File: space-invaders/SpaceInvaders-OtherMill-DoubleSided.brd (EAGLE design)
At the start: 101.6 x 95.2 mm, 26 parts, among them J2-J4 TM4C123GXL, J3-J1 TM4C123GXL, J5 Nokia_5110, J6 Nokia_5110, J7 9V, U1 LM7805CT

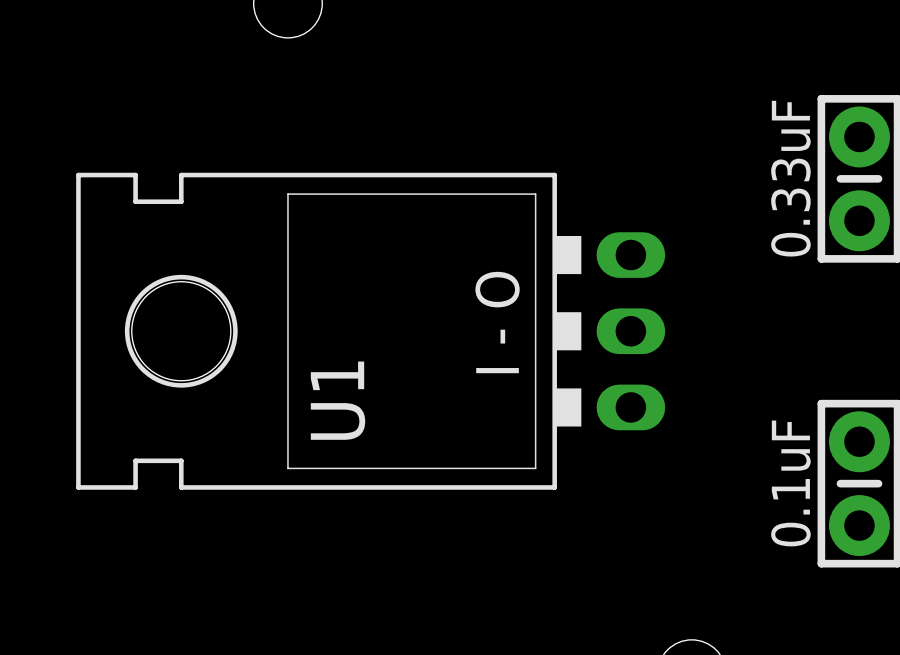
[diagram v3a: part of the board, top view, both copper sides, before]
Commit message: Connect nets & Apply schematic convention
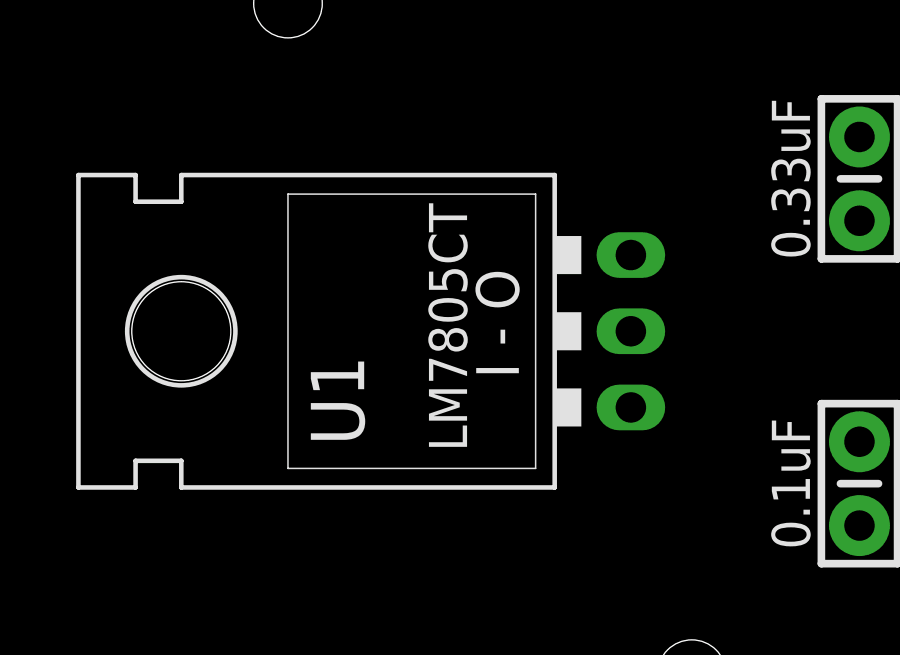
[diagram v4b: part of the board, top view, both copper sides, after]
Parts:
- J5, J6: value Nokia_5110 -> NOKIA_5110
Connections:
- removed net D/C: J6.5
- removed net DN<MOSI>: J6.6
- removed net PE0: J2-J4.6, R2.P$2, S2.3
- removed net RST: J6.4
- removed net SCE: J5.3
- removed net SCLK: J5.7
- new net DAC: J2-J4.4, J2-J4.5, J3-J1.14, J3-J1.16, R10.P$1, R11.P$1, R6.P$1, R7.P$1, R9.P$1
- net PA2: now also J5.7
- net PA3: now also J5.3
- net PA5: now also J6.6
- net PA6: now also J6.5
- net PA7: now also J6.4
- net PB2: now also J2-J4.6, R2.P$2, S2.3; no longer J2-J4.4, J2-J4.5, J3-J1.14, J3-J1.16, R10.P$1, R11.P$1, R6.P$1, R7.P$1, R9.P$1
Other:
- board text added: "LM7805CT"
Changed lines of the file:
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@@
 <?xml version="1.0" encoding="utf-8"?>
 <!DOCTYPE eagle SYSTEM "eagle.dtd">
-<eagle version="8.0.0">
+<eagle version="8.0.1">
 <drawing>
 <settings>
@@
 <text x="77.47" y="57.15" size="1.27" layer="21" font="vector" ratio="10" align="center">220</text>
 <text x="23.495" y="80.264" size="1.4224" layer="21" font="vector" ratio="10" rot="R90" align="center">I - O</text>
+<text x="21.844" y="80.137" size="1.27" layer="21" ratio="10" rot="R90" align="center">LM7805CT</text>
 </plain>
 <attributes>
@@
 <autorouter>
 <pass name="Default">
-<param name="RoutingGrid" value="6.25mil"/>
+<param name="RoutingGrid" value="50mil"/>
 <param name="AutoGrid" value="1"/>
 <param name="Efforts" value="2"/>
 <param name="TopRouterVariant" value="1"/>
 <param name="tpViaShape" value="round"/>
-<param name="PrefDir.1" value="*"/>
+<param name="PrefDir.1" value="a"/>
 <param name="PrefDir.2" value="0"/>
 <param name="PrefDir.3" value="0"/>
@@
 <param name="PrefDir.14" value="0"/>
 <param name="PrefDir.15" value="0"/>
-<param name="PrefDir.16" value="-"/>
+<param name="PrefDir.16" value="a"/>
 <param name="cfVia" value="8"/>
 <param name="cfNonPref" value="5"/>
@@
 <element name="J2-J4" library="SparkFun-Connectors" package="2X10" value="TM4C123GXL" x="48.26" y="63.5" rot="R270"/>
 <element name="J3-J1" library="SparkFun-Connectors" package="2X10" value="TM4C123GXL" x="7.62" y="40.64" rot="R90"/>
-<element name="J5" library="SparkFun-Connectors" package="1X08" value="Nokia_5110" x="68.58" y="71.12">
+<element name="J5" library="SparkFun-Connectors" package="1X08" value="NOKIA_5110" x="68.58" y="71.12">
 <attribute name="PROD_ID" value="CONN-08438" x="68.58" y="71.12" size="1.778" layer="27" display="off"/>
 </element>
-<element name="J6" library="SparkFun-Connectors" package="1X08" value="Nokia_5110" x="68.58" y="30.48">
+<element name="J6" library="SparkFun-Connectors" package="1X08" value="NOKIA_5110" x="68.58" y="30.48">
 <attribute name="PROD_ID" value="CONN-08438" x="68.58" y="30.48" size="1.778" layer="27" display="off"/>
 </element>
@@
 <contactref element="J6" pad="7"/>
 <contactref element="J2-J4" pad="20"/>
+<contactref element="J5" pad="7"/>
+<wire x1="83.82" y1="30.48" x2="83.82" y2="71.12" width="0" layer="19" extent="1-1"/>
 <wire x1="50.8" y1="40.64" x2="83.82" y2="30.48" width="0" layer="19" extent="1-1"/>
 </signal>
@@
 <contactref element="J3-J1" pad="2"/>
 <contactref element="J5" pad="4"/>
-<wire x1="5.08" y1="40.64" x2="76.2" y2="71.12" width="0" layer="19" extent="1-1"/>
+<contactref element="J6" pad="4"/>
+<wire x1="76.2" y1="30.48" x2="76.2" y2="71.12" width="0" layer="19" extent="1-1"/>
+<wire x1="5.08" y1="40.64" x2="76.2" y2="30.48" width="0" layer="19" extent="1-1"/>
 </signal>
 <signal name="PA6">
 <contactref element="J3-J1" pad="4"/>
 <contactref element="J5" pad="5"/>
-<wire x1="5.08" y1="43.18" x2="78.74" y2="71.12" width="0" layer="19" extent="1-1"/>
+<contactref element="J6" pad="5"/>
+<wire x1="78.74" y1="30.48" x2="78.74" y2="71.12" width="0" layer="19" extent="1-1"/>
+<wire x1="5.08" y1="43.18" x2="78.74" y2="30.48" width="0" layer="19" extent="1-1"/>
 </signal>
 <signal name="PA5">
 <contactref element="J3-J1" pad="6"/>
 <contactref element="J5" pad="6"/>
-<wire x1="5.08" y1="45.72" x2="81.28" y2="71.12" width="0" layer="19" extent="1-1"/>
+<contactref element="J6" pad="6"/>
+<wire x1="81.28" y1="30.48" x2="81.28" y2="71.12" width="0" layer="19" extent="1-1"/>
+<wire x1="5.08" y1="45.72" x2="81.28" y2="30.48" width="0" layer="19" extent="1-1"/>
 </signal>
 <signal name="PB4">
@@
 <wire x1="5.08" y1="48.26" x2="80.01" y2="25.4" width="0" layer="19" extent="1-1"/>
 </signal>
-<signal name="PB2">
+<signal name="DAC">
 <contactref element="R6" pad="P$1"/>
 <contactref element="R7" pad="P$1"/>
@@
 <contactref element="J6" pad="3"/>
 <contactref element="J2-J4" pad="18"/>
-<wire x1="50.8" y1="43.18" x2="73.66" y2="30.48" width="0" layer="19" extent="1-1"/>
+<contactref element="J5" pad="3"/>
+<wire x1="50.8" y1="43.18" x2="73.66" y2="71.12" width="0" layer="19" extent="1-1"/>
+<wire x1="73.66" y1="30.48" x2="50.8" y2="43.18" width="0" layer="19" extent="1-1"/>
 </signal>
 <signal name="3.3V" class="1">
@@
 <contactref element="J3-J1" pad="15"/>
 </signal>
-<signal name="RST">
-<contactref element="J6" pad="4"/>
-</signal>
-<signal name="D/C">
-<contactref element="J6" pad="5"/>
-</signal>
-<signal name="DN&lt;MOSI&gt;">
-<contactref element="J6" pad="6"/>
-</signal>
-<signal name="SCE">
-<contactref element="J5" pad="3"/>
-</signal>
-<signal name="SCLK">
-<contactref element="J5" pad="7"/>
-</signal>
 <signal name="PF2">
 <contactref element="J2-J4" pad="1"/>
@@
 <wire x1="7.62" y1="48.26" x2="84.3788" y2="5.3594" width="0" layer="19" extent="1-1"/>
 </signal>
-<signal name="PE0">
+<signal name="PB2">
 <contactref element="R2" pad="P$2"/>
 <contactref element="J2-J4" pad="6"/>

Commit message: Expand & make more space in schematic
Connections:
- net PB2 renamed PE0
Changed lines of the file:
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@@
 </signal>
 <signal name="DAC_OUT">
-<contactref element="R6" pad="P$2"/>
-<contactref element="R8" pad="P$2"/>
 <contactref element="R9" pad="P$2"/>
 <contactref element="R10" pad="P$2"/>
 <contactref element="R11" pad="P$2"/>
+<contactref element="R6" pad="P$2"/>
+<contactref element="R8" pad="P$2"/>
 <contactref element="LS1" pad="+"/>
 <wire x1="25.4" y1="30.48" x2="45.01" y2="20.32" width="0" layer="19" extent="1-1"/>
@@
 <signal name="DAC">
 <contactref element="R6" pad="P$1"/>
-<contactref element="R7" pad="P$1"/>
-<contactref element="R9" pad="P$1"/>
-<contactref element="R10" pad="P$1"/>
-<contactref element="R11" pad="P$1"/>
 <contactref element="J2-J4" pad="5"/>
 <contactref element="J2-J4" pad="4"/>
 <contactref element="J3-J1" pad="14"/>
 <contactref element="J3-J1" pad="16"/>
+<contactref element="R7" pad="P$1"/>
+<contactref element="R9" pad="P$1"/>
+<contactref element="R11" pad="P$1"/>
+<contactref element="R10" pad="P$1"/>
 <wire x1="48.26" y1="58.42" x2="50.8" y2="60.96" width="0" layer="19" extent="1-1"/>
 <wire x1="5.08" y1="58.42" x2="48.26" y2="58.42" width="0" layer="19" extent="1-1"/>
@@
 <wire x1="7.62" y1="48.26" x2="84.3788" y2="5.3594" width="0" layer="19" extent="1-1"/>
 </signal>
-<signal name="PB2">
+<signal name="PE0">
 <contactref element="R2" pad="P$2"/>
 <contactref element="J2-J4" pad="6"/>

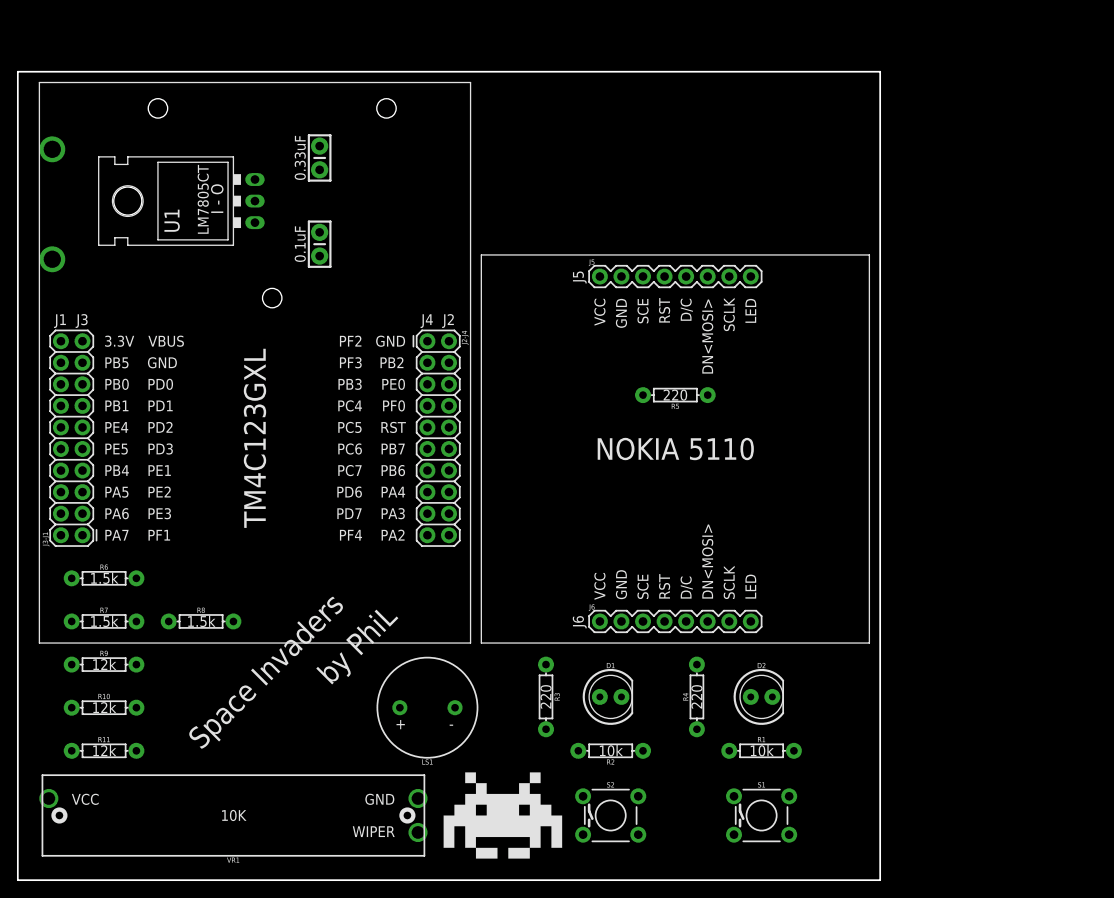
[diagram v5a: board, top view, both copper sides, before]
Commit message: Minimize the board area to 3.60" x 3.60"
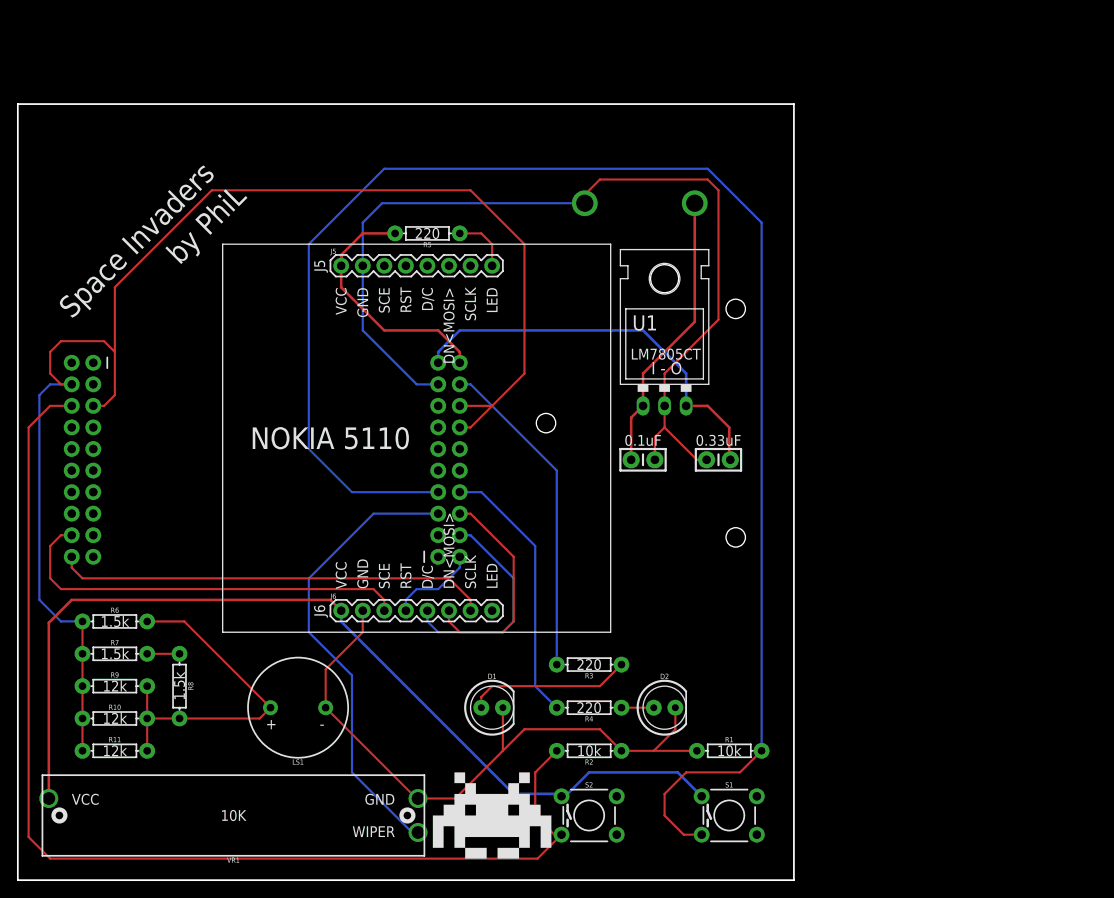
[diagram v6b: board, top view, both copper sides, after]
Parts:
- moved C1 58.9 mm to (82.5, 49.5), turned to 0 degrees
- moved U1 55.9 mm to (76.2, 59.7), turned to 0 degrees
- moved C2 45.8 mm to (73.7, 49.5), turned to 0 degrees
- moved J3-J1 42.0 mm to (49.5, 38.1), flipped to the bottom
- moved J2-J4 39.5 mm to (8.89, 61.0), flipped to the bottom
- moved J7 38.1 mm to (58.4, 26.7), turned to 90 degrees
- moved R5 34.9 mm to (48.3, 76.2)
- moved J5 30.5 mm to (38.1, 72.4)
- moved J6 30.5 mm to (38.1, 31.8)
- moved LS1 15.2 mm to (33.0, 20.3)
- moved D1 14.0 mm to (55.9, 20.3)
- moved R4 12.8 mm to (67.3, 20.3), turned to 180 degrees
- moved D2 11.5 mm to (76.2, 20.3)
- moved R8 8.03 mm to (19.1, 22.9), turned to 270 degrees
- moved R3 6.35 mm to (67.3, 25.4), turned to 180 degrees
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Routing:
- net GND: track 0.00 -> 187.8 mm
- net PE1: track 0.00 -> 184.7 mm
- net DAC: track 0.00 -> 164.8 mm
- net 3.3V: track 0.00 -> 142.3 mm
- net PE0: track 0.00 -> 132.1 mm
- net PE2: track 0.00 -> 54.1 mm
- net PA2: track 0.00 -> 51.1 mm
- net PA3: track 0.00 -> 48.6 mm
- net VBUS: track 0.00 -> 47.4 mm
- net DAC_OUT: track 0.00 -> 41.4 mm
- net PB5: track 0.00 -> 38.5 mm
- net 9V: track 0.00 -> 33.3 mm
- net PB4: track 0.00 -> 31.6 mm
- net PA6: track 0.00 -> 26.0 mm
- net PA5: track 0.00 -> 26.0 mm
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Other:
- board size 101.6 x 95.2 mm -> 91.4 x 91.4 mm
